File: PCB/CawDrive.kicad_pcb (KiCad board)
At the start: 4 copper layers, 42 x 42 mm, 84 parts, among them CN1 WAFER-SH1.0-6PWB, CN2 WAFER-SH1.0-6PWB, Q10 TPH3R704PL, Q11 TPH3R704PL, Q12 TPH3R704PL, Q7 TPH3R704PL, Q8 TPH3R704PL, Q9 TPH3R704PL, U1 AS5047P-ATSM, U2 TLV76733DRVR, U3 TCAN1044DRBRQ1, U4 STM32G474RETx, U5 WAFER-SH1.0-2PWB, U6 WAFER-SH1.0-2PWB, U7 DRV8323RSRGZR, X1 Crystal_16MHz_15pF_3P

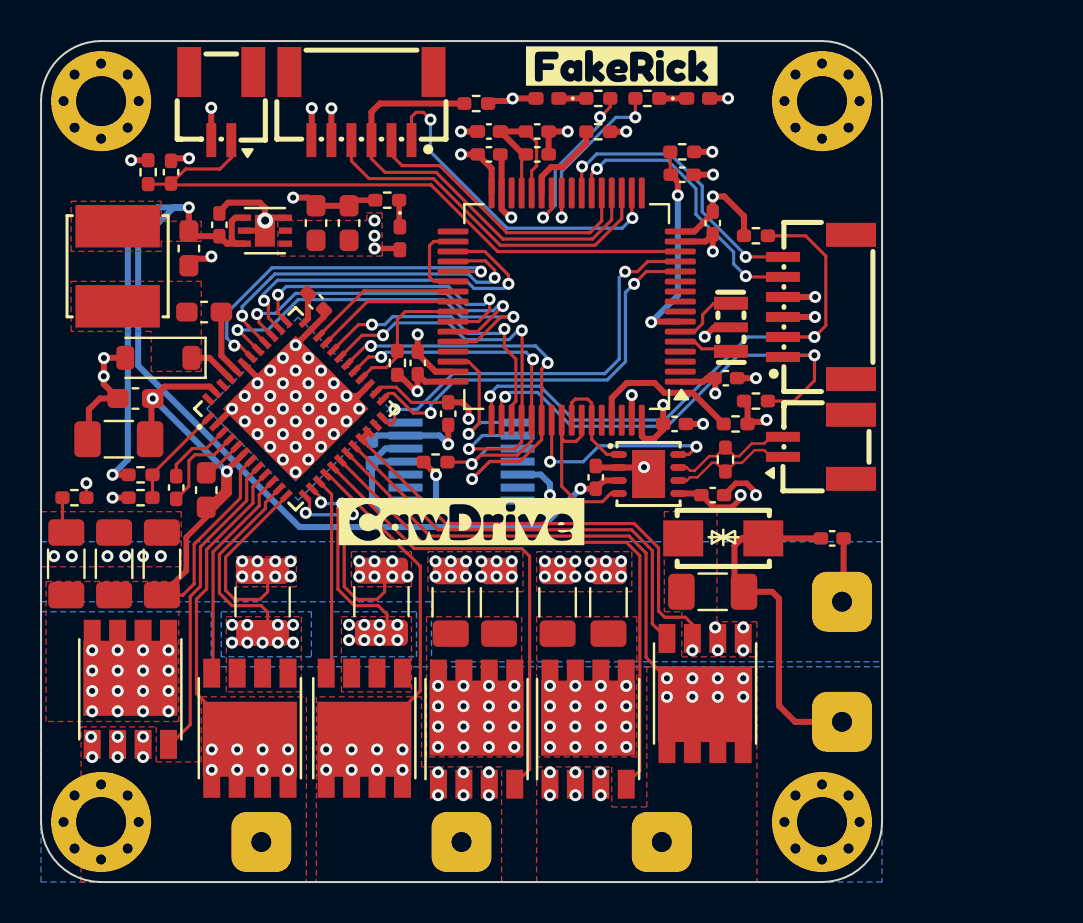
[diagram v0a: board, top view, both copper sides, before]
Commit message: 升级V2版，支持3路电流采样以及霍尔传感器
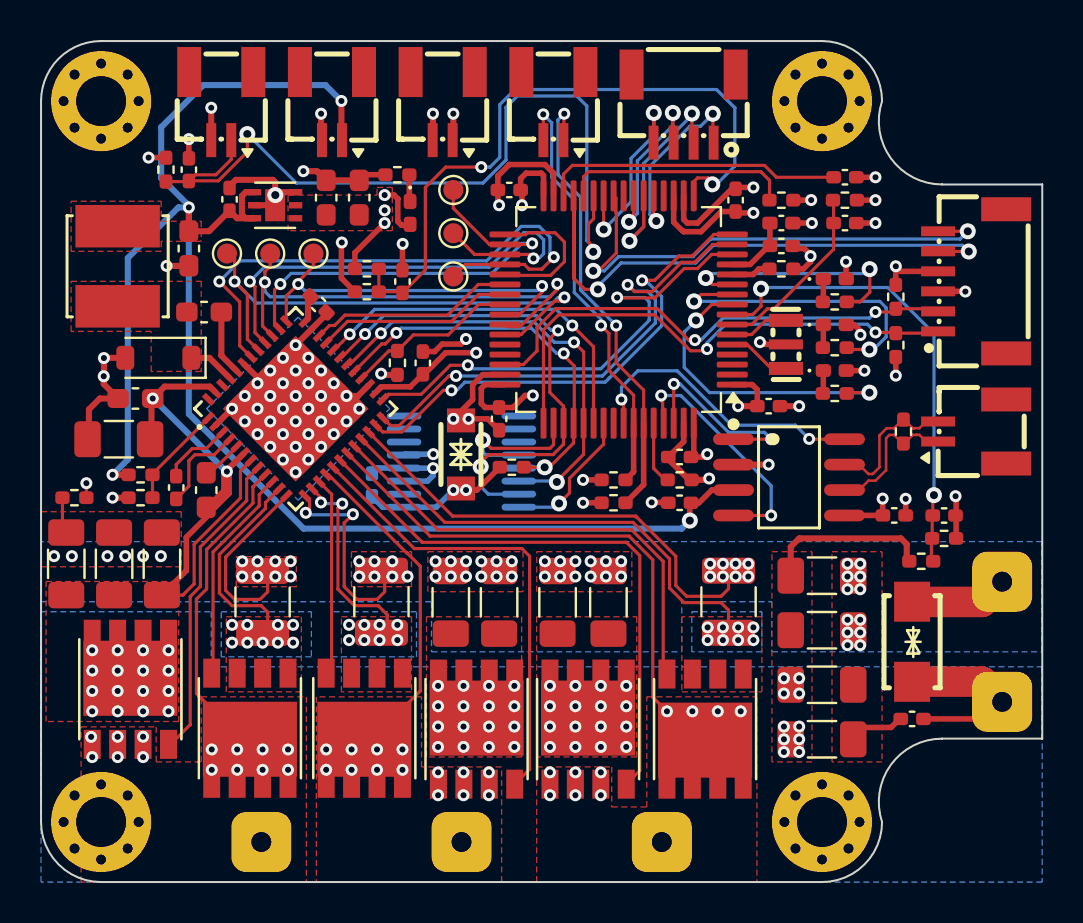
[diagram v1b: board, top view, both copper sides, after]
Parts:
- removed C8: 0.1uF, Capacitor_SMD:C_0402_1005Metric_Pad0.74x0.62mm_HandSolder
- removed CN1: WAFER-SH1.0-6PWB, Rick_Connector:CONN-SMD_6P-P1.00_XUNPU_WAFER-SH1.0-6PWB
- removed U3: TCAN1044DRBRQ1, Rick_CAN:TCAN1044DRBRQ1_DFN-8_L3.0-W3.0-P0.65-TL-EP2.4
- removed U4: STM32G474RETx, Package_QFP:LQFP-64_10x10mm_P0.5mm
- removed kibuzzard-66ADBF8B: G***, kibuzzard-66ADBF8B
- removed kibuzzard-66ADCBBA: G***, kibuzzard-66ADCBBA
- added C13: 0.1uF, Capacitor_SMD:C_0402_1005Metric_Pad0.74x0.62mm_HandSolder, F.Cu at (151.9, 91.1)
- added C18: 0.1uF, Capacitor_SMD:C_0402_1005Metric_Pad0.74x0.62mm_HandSolder, B.Cu at (136.5, 90.2)
- added C19: 33nF, Capacitor_SMD:C_0402_1005Metric_Pad0.74x0.62mm_HandSolder, F.Cu at (165.1, 91.7)
- added C36: 10uF/50V, Capacitor_SMD:C_1206_3216Metric_Pad1.33x1.80mm_HandSolder, F.Cu at (159.0, 97.4)
- added C37: 10uF/50V, Capacitor_SMD:C_1206_3216Metric_Pad1.33x1.80mm_HandSolder, F.Cu at (159.0, 100.1)
- added C38: 10uF/50V, Capacitor_SMD:C_1206_3216Metric_Pad1.33x1.80mm_HandSolder, F.Cu at (159.0, 102.9)
- added CN3: WAFER-SH1.0-4PWB, Rick_Connector:CONN-SMD_4P-P1.00_WAFER-SH1.0-4PWB, F.Cu at (152.1, 71.4)
- added D5: SMF6.0CA_C2836402, Rick_Diode:SMF6.0CA_SOD-123FL_L2.8-W1.8-LS3.7-BI, F.Cu at (141.0, 88.6)
- added D6: ENCODER_STA_LED, LED_SMD:LED_0402_1005Metric_Pad0.77x0.64mm_HandSolder, F.Cu at (159.6, 84.5)
- added R22: 1mΩ 1%, Resistor_SMD:R_1210_3225Metric_Pad1.30x2.65mm_HandSolder, F.Cu at (154.3, 96.0)
- added R23: 10K, Resistor_SMD:R_0402_1005Metric_Pad0.72x0.64mm_HandSolder, F.Cu at (151.9, 89.9)
- added R24: 0Ω, Resistor_SMD:R_0402_1005Metric_Pad0.72x0.64mm_HandSolder, F.Cu at (157.0, 79.4)
- added R25: 10K, Resistor_SMD:R_0402_1005Metric_Pad0.72x0.64mm_HandSolder, F.Cu at (157.0, 75.9)
- added R26: 120Ω 1%, Resistor_SMD:R_0402_1005Metric_Pad0.72x0.64mm_HandSolder, F.Cu at (163.1, 87.5)
- added R3: 10k, Resistor_SMD:R_0402_1005Metric_Pad0.72x0.64mm_HandSolder, F.Cu at (162.7, 83.2)
- added R5: 10k, Resistor_SMD:R_0402_1005Metric_Pad0.72x0.64mm_HandSolder, F.Cu at (148.6, 89.9)
- added R6: 10k, Resistor_SMD:R_0402_1005Metric_Pad0.72x0.64mm_HandSolder, F.Cu at (148.6, 91.1)
- added TP1: TestPoint, TestPoint:TestPoint_Pad_D1.0mm, F.Cu at (140.6, 75.4)
- added TP2: TestPoint, TestPoint:TestPoint_Pad_D1.0mm, F.Cu at (140.6, 77.6)
- added TP3: TestPoint, TestPoint:TestPoint_Pad_D1.0mm, F.Cu at (140.6, 79.8)
- added TP4: TestPoint, TestPoint:TestPoint_Pad_D1.0mm, F.Cu at (133.6, 78.6)
- added TP5: TestPoint, TestPoint:TestPoint_Pad_D1.0mm, F.Cu at (131.4, 78.6)
- added TP6: TestPoint, TestPoint:TestPoint_Pad_D1.0mm, F.Cu at (129.3, 78.6)
- added U10: WAFER-SH1.0-2PWB, Rick_Connector:CONN-SMD_2P-P1.00_XUNPU_WAFER-SH1.0-2PWB, F.Cu at (145.6, 71.2)
- added U11: WAFER-SH1.0-2PWB, Rick_Connector:CONN-SMD_2P-P1.00_XUNPU_WAFER-SH1.0-2PWB, F.Cu at (134.5, 71.2)
- added U12: WAFER-SH1.0-2PWB, Rick_Connector:CONN-SMD_2P-P1.00_XUNPU_WAFER-SH1.0-2PWB, F.Cu at (140.1, 71.2)
- added U8: STM32F446RETx, Package_QFP:LQFP-64_10x10mm_P0.5mm, F.Cu at (148.8, 81.4)
- added U9: MT6835GT-STD, Rick_Sensor:MT6835GT-STD, B.Cu at (141.0, 89.0)
- added kibuzzard-67F13BB6: G***, kibuzzard-67F13BB6, B.Cu at (163.0, 89.0)
- C17: moved to F.Cu
- C9: value 0.1uF -> 2.2uF
- R11, R7, R9: value 510 -> 510Ω
- R12: value 10K -> 3k
- R15: value 0Ω -> 510Ω
- R8: value 120Ω 1% -> 75k
- U1: value AS5047P-ATSM -> TJA1051T/3/1J; footprint Rick_Sensor:AS5047P-ATSM -> Rick_CAN:TJA1051T31J_SOIC-8_L4.9-W3.9-P1.27-LS6.0-BL; moved to F.Cu
- X1: value Crystal_16MHz_15pF_3P -> CSTNE16M0V530000R0
- moved C17 26.3 mm to (162.6, 91.7), turned to 180 degrees
- moved R2 23.1 mm to (162.7, 80.8), turned to 90 degrees
- moved R21 20.2 mm to (136.3, 80.5), turned to 0 degrees
- moved R20 19.5 mm to (136.3, 79.4)
- moved R15 17.6 mm to (159.6, 85.6)
- moved C9 17.2 mm to (160.1, 74.8)
- moved D1 16.9 mm to (159.6, 79.9), turned to 0 degrees
- moved U1 16.4 mm to (157.4, 89.8)
- moved R9 15.6 mm to (159.6, 81.0)
- moved R11 15.6 mm to (159.6, 83.3), turned to 0 degrees
- moved L1 15.3 mm to (157.0, 77.1), turned to 180 degrees
- moved C12 13.7 mm to (138.0, 80.0)
- moved C11 13.5 mm to (157.0, 78.2)
- moved D2 13.2 mm to (159.6, 82.2)
- moved R12 11.9 mm to (165.1, 92.8), turned to 180 degrees
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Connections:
- net /ADC1_IN3 renamed /ADC2_IN9
- C12 pad 2: +5V -> /ADC3_IN3
- C9 pad 2: +3.3V -> Net-(U8-VCAP_1)
- CN2 pad 5: /USART1_TX -> /USART3_TX
- CN2 pad 6: /USART1_RX -> /USART3_RX
- Q12 pad 1: GND1 -> /DRV8323RSRGZR/SPC
- Q12 pad 2: GND1 -> /DRV8323RSRGZR/SPC
- Q12 pad 3: GND1 -> /DRV8323RSRGZR/SPC
- R12 pad 1: Net-(U4-PB8) -> GND
- R12 pad 2: GND -> /ADC1_IN10
- R15 pad 2: GND -> /ENCODER_STA
- R2 pad 1: +3.3V -> /SWDIO
- R2 pad 2: /SPI1_MISO -> +3.3V
- R20 pad 1: /SWDIO -> /ADC3_IN3
- R21 pad 1: /SWCLK -> GND
- R21 pad 2: GND -> /ADC3_IN3
- R8 pad 1: /CAN_N -> /ADC1_IN10
- R8 pad 2: /CAN_P -> +36V
- U1 pad 1: /AS5047P_NSS -> /CAN_TX
- U1 pad 2: /SPI3_SCK -> GND
- U1 pad 3: /SPI3_MISO -> +5V
- U1 pad 4: /SPI3_MOSI -> /CAN_RX
- U1 pad 5: GND -> +3.3V
- U1 pad 6: unconnected-(U1-B-Pad6) -> /CAN_N
- U1 pad 7: unconnected-(U1-A-Pad7) -> /CAN_P
- U1 pad 8: unconnected-(U1-W/PWM-Pad8) -> /CAN_STB
- U7 pad 21: GND1 -> /DRV8323RSRGZR/SPC
- U7 pad 23: unconnected-(U7-SOC-Pad23) -> /ADC3_IN2
- U7 pad 24: /ADC1_IN2 -> /ADC2_IN1
- U7 pad 25: /ADC1_IN1 -> /ADC1_IN0
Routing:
- net /ADC3_IN3: track 0.00 -> 33.7 mm, vias 0 -> 2
- net /USART3_TX: track 0.00 -> 26.7 mm, vias 0 -> 2
- net /USART3_RX: track 0.00 -> 25.4 mm, vias 0 -> 2
- net /ADC2_IN1: track 0.00 -> 25.1 mm, vias 0 -> 2
- net /ADC3_IN2: track 0.00 -> 24.8 mm, vias 0 -> 2
- net /ADC1_IN0: track 0.00 -> 24.3 mm, vias 0 -> 2
- net /DRV8323RSRGZR/SPC: track 0.00 -> 23.8 mm, vias 0 -> 8
- net /ADC1_IN10: track 0.00 -> 23.3 mm, vias 0 -> 2
- net /I2C1_SDA: track 0.00 -> 23.0 mm, vias 0 -> 2
- net /I2C1_SCL: track 0.00 -> 21.6 mm, vias 0 -> 2
- net /ADC1_IN2: track 21.1 -> 0.00 mm, vias 2 -> 0
- net /ADC1_IN1: track 20.6 -> 0.00 mm, vias 2 -> 0
- net +5V: track 60.9 -> 81.2 mm, vias 3 -> 4
- net GND: track 63.3 -> 79.2 mm, vias 62 -> 69
- net /ENCODER_STA: track 0.00 -> 15.6 mm, vias 0 -> 2
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- added copper zone on In1.Cu, net +36V
- added copper zone on B.Cu, net /DRV8323RSRGZR/SPC
- added copper zone on F.Cu, net /DRV8323RSRGZR/SPC
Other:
- board size 42 x 42 mm -> 50 x 42 mm

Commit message: 增加测试点PC13引脚
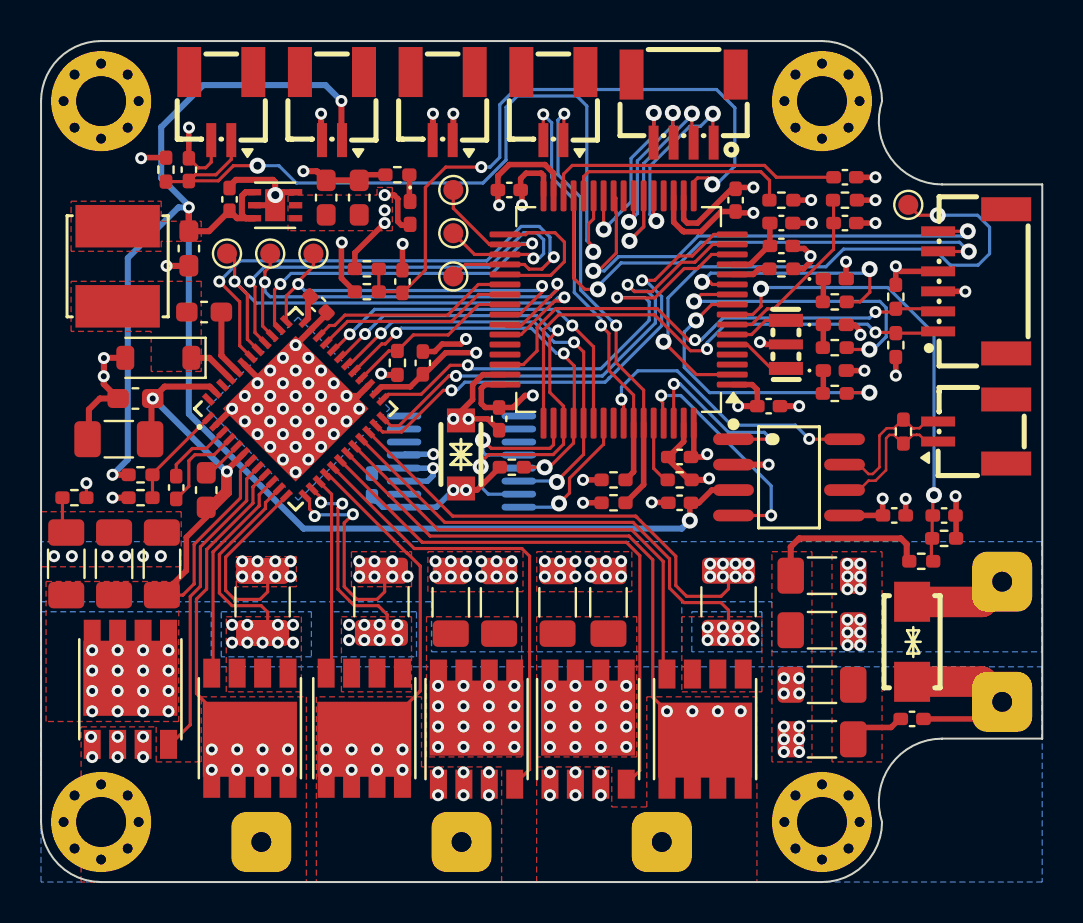
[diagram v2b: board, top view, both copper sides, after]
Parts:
- added TP7: TestPoint, TestPoint:TestPoint_Pad_D1.0mm, F.Cu at (163.3, 76.2)
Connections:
- U8 pad 2: unconnected-(U8-PC13-Pad2) -> Net-(U8-PC13)
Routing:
- net Net-(U8-PC13): track 0.00 -> 29.9 mm, vias 0 -> 2
- net /ADC2_IN9: track 41.0 -> 39.1 mm
- net GND: track 79.2 -> 80.7 mm, vias 69 -> 68
